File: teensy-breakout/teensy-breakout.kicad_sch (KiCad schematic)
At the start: 78 parts, among them J1 USB_B, J10 Conn_01x04, J11 Conn_01x04, J12 Conn_01x05, J13 Conn_01x03, J14 Conn_01x04, J15 Conn_01x04, J16 Conn_01x02, J17 Conn_01x08, J18 Conn_01x08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

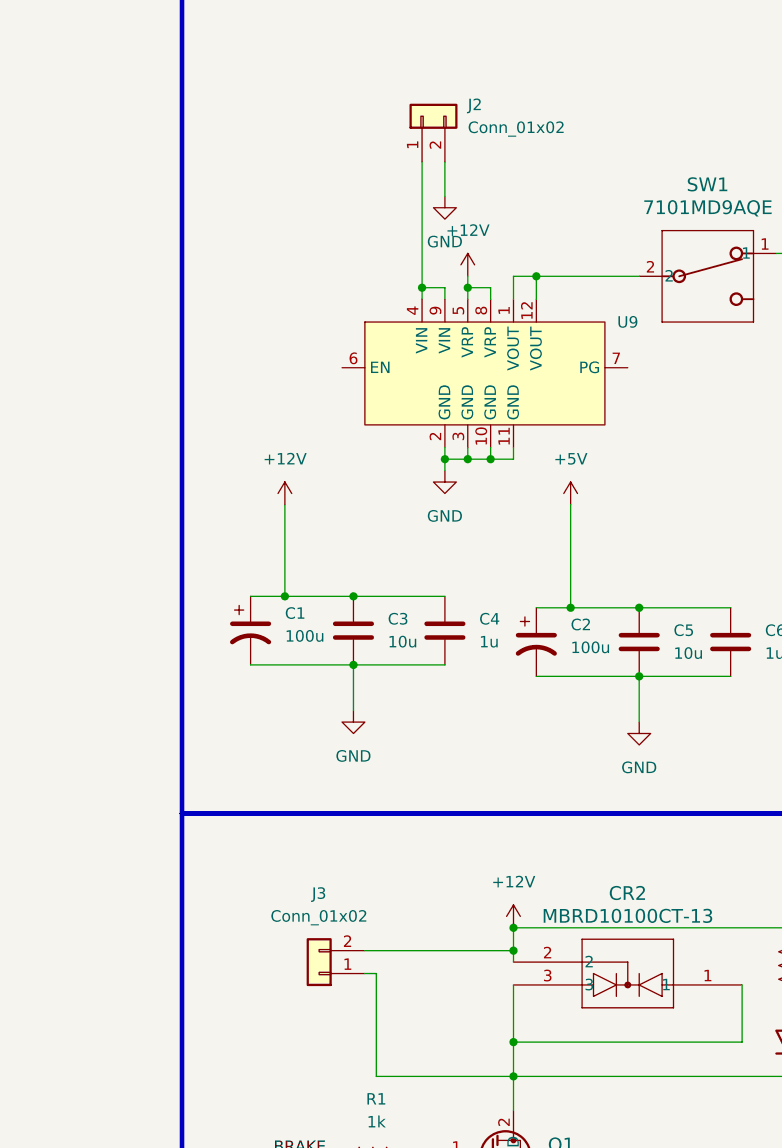
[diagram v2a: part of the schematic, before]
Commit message: Added rest of silkscreen
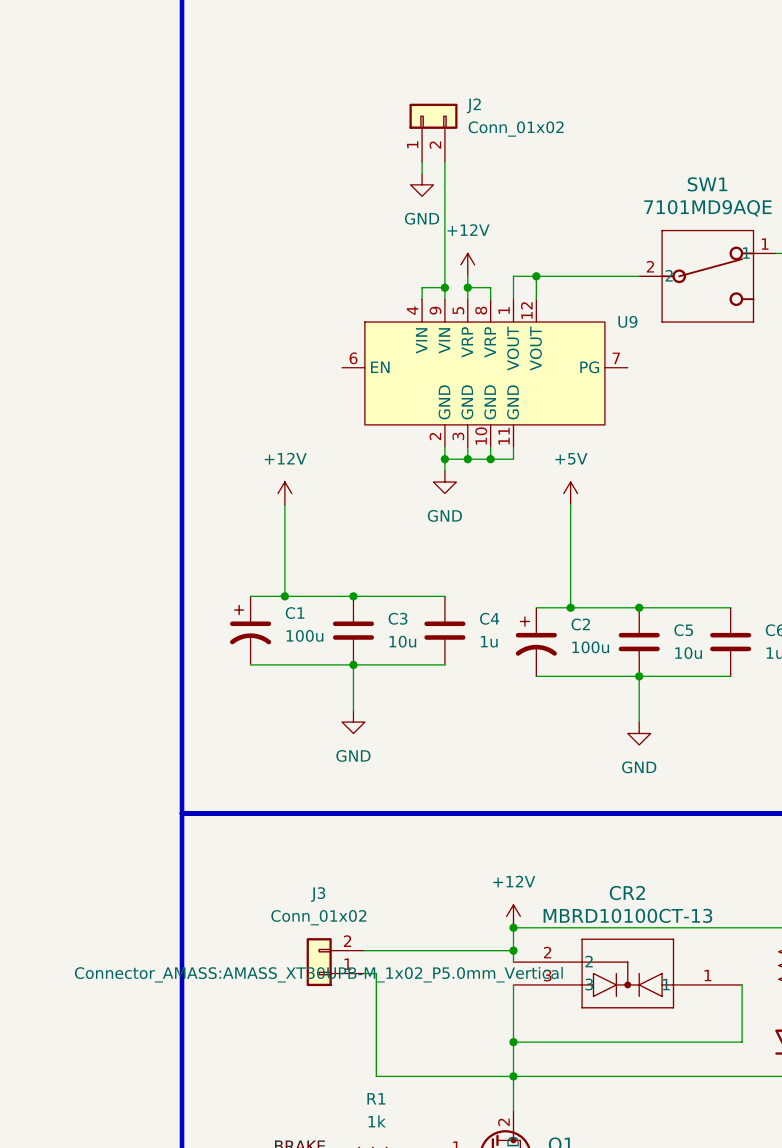
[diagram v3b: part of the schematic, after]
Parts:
- J2, J3: footprint Connector_AMASS:AMASS_XT60-F_1x02_P7.20mm_Vertical -> Connector_AMASS:AMASS_XT30UPB-M_1x02_P5.0mm_Vertical
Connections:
- net GND: now also J2.1 (Pin_1); no longer J2.2 (Pin_2)
- net at U9.4 (VIN), U9.9 (VIN): now also J2.2 (Pin_2); no longer J2.1 (Pin_1)
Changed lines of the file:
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@@
 	)
 	(junction
-		(at 38.1 48.26)
-		(diameter 0)
-		(color 0 0 0 0)
-	)
-	(junction
 		(at 22.86 82.55)
 		(diameter 0)
@@
 	)
 	(junction
+		(at 40.64 48.26)
+		(diameter 0)
+		(color 0 0 0 0)
+	)
+	(junction
 		(at 182.88 82.55)
 		(diameter 0)
@@
 	(wire
 		(pts
+			(xy 40.64 34.29) (xy 40.64 48.26)
+		)
+		(stroke
+			(width 0)
+			(type default)
+		)
+	)
+	(wire
+		(pts
 			(xy 341.63 177.8) (xy 350.52 177.8)
 		)
@@
 	(wire
 		(pts
-			(xy 40.64 34.29) (xy 40.64 38.1)
-		)
-		(stroke
-			(width 0)
-			(type default)
-		)
-	)
-	(wire
-		(pts
 			(xy 224.79 36.83) (xy 224.79 21.59)
 		)
@@
 	(wire
 		(pts
+			(xy 38.1 34.29) (xy 38.1 35.56)
+		)
+		(stroke
+			(width 0)
+			(type default)
+		)
+	)
+	(wire
+		(pts
 			(xy 176.53 240.03) (xy 185.42 240.03)
 		)
@@
 	(wire
 		(pts
-			(xy 38.1 34.29) (xy 38.1 48.26)
-		)
-		(stroke
-			(width 0)
-			(type default)
-		)
-	)
-	(wire
-		(pts
 			(xy 48.26 135.89) (xy 78.74 135.89)
 		)
@@
 			)
 		)
-		(property "Footprint" "Connector_AMASS:AMASS_XT60-F_1x02_P7.20mm_Vertical"
+		(property "Footprint" "Connector_AMASS:AMASS_XT30UPB-M_1x02_P5.0mm_Vertical"
 			(at 38.1 29.21 0)
 			(effects
@@
 	(symbol
 		(lib_id "power:GND")
-		(at 40.64 38.1 0)
+		(at 38.1 35.56 0)
 		(unit 1)
 		(exclude_from_sim no)
@@
 		(fields_autoplaced yes)
 		(property "Reference" "#PWR0102"
-			(at 40.64 44.45 0)
+			(at 38.1 41.91 0)
 			(effects
 				(font
@@
 		)
 		(property "Value" "GND"
-			(at 40.64 43.18 0)
+			(at 38.1 40.64 0)
 			(effects
 				(font
@@
 		)
 		(property "Footprint" ""
-			(at 40.64 38.1 0)
+			(at 38.1 35.56 0)
 			(effects
 				(font
@@
 		)
 		(property "Datasheet" ""
-			(at 40.64 38.1 0)
+			(at 38.1 35.56 0)
 			(effects
 				(font
@@
 		)
 		(property "Description" "Power symbol creates a global label with name \"GND\" , ground"
-			(at 40.64 38.1 0)
+			(at 38.1 35.56 0)
 			(effects
 				(font
@@
 			)
 		)
-		(property "Footprint" "Connector_AMASS:AMASS_XT60-F_1x02_P7.20mm_Vertical"
+		(property "Footprint" "Connector_AMASS:AMASS_XT30UPB-M_1x02_P5.0mm_Vertical"
 			(at 26.67 124.46 0)
 			(effects
@@
 					(size 1.27 1.27)
 				)
-				(hide yes)
 			)
 		)
